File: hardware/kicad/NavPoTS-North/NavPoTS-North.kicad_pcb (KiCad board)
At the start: 4 copper layers, 58.9 x 58.9 mm, 52 parts, among them J1 DM3CS-SF, J10 Conn_02x04_Top_Bottom, J2 Conn_Coaxial, J3 Conn_Coaxial, J4 Conn_02x04_Top_Bottom, J5 Conn_01x02, J6 Conn_02x04_Top_Bottom, J7 62684-402100ALF, J8 Conn_02x04_Top_Bottom, J9 Conn_01x02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

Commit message: v1.0
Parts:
- U3: footprint custom:NEO-M8N -> RF_GPS:ublox_NEO
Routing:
- net GND: vias 1 -> 23
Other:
- board text added: "v1.0 - 6/13/26 Luke Hooper"

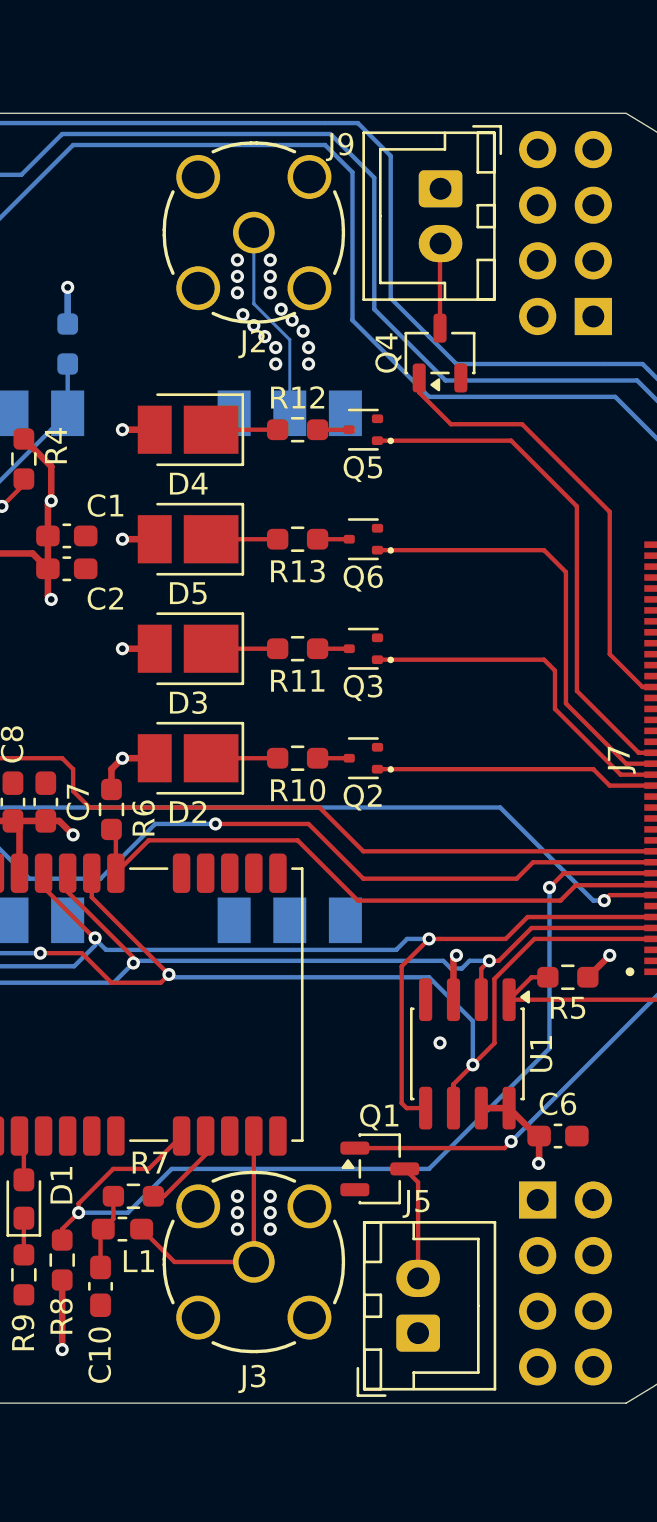
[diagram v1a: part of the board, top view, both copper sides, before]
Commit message: update to kicad, begin cad work for pcb holder bracket
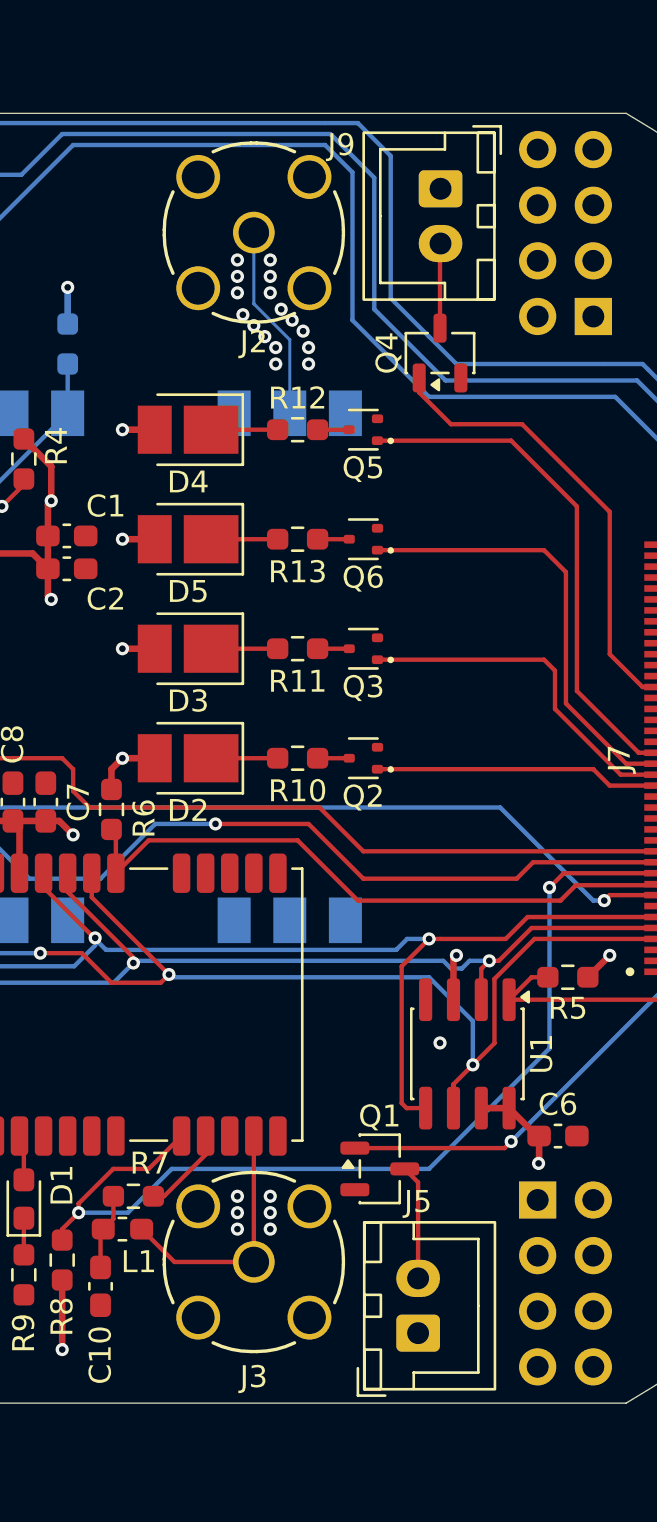
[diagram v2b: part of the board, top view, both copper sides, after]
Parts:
- D2, D3, D4, D5: footprint LED_SMD:LED_PLCC_2835_Handsoldering -> custom:LED_PLCC_2835_Handsoldering
- U3: footprint RF_GPS:ublox_NEO -> custom:NEO-M8N
